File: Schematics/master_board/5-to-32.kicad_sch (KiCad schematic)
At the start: 22 parts, among them J10 Conn_01x06_Male, J11 Conn_01x06_Male, J12 Conn_01x06_Male, J13 Conn_01x06_Male, J14 Conn_01x06_Male, J15 Conn_01x06_Male, J16 Conn_01x06_Male, J17 Conn_01x06_Male, J18 Conn_01x06_Male, J19 Conn_01x06_Male, J20 Conn_01x06_Male, J21 Conn_01x06_Male, J22 Conn_01x06_Male, J23 Conn_01x06_Male, J24 Conn_01x06_Male, J25 Conn_01x06_Male, J26 Conn_01x06_Male, J7 Conn_01x06_Male, J8 Conn_01x06_Male, J9 Conn_01x06_Male, U4 74HCT154PW,118, U5 74HCT154PW,118

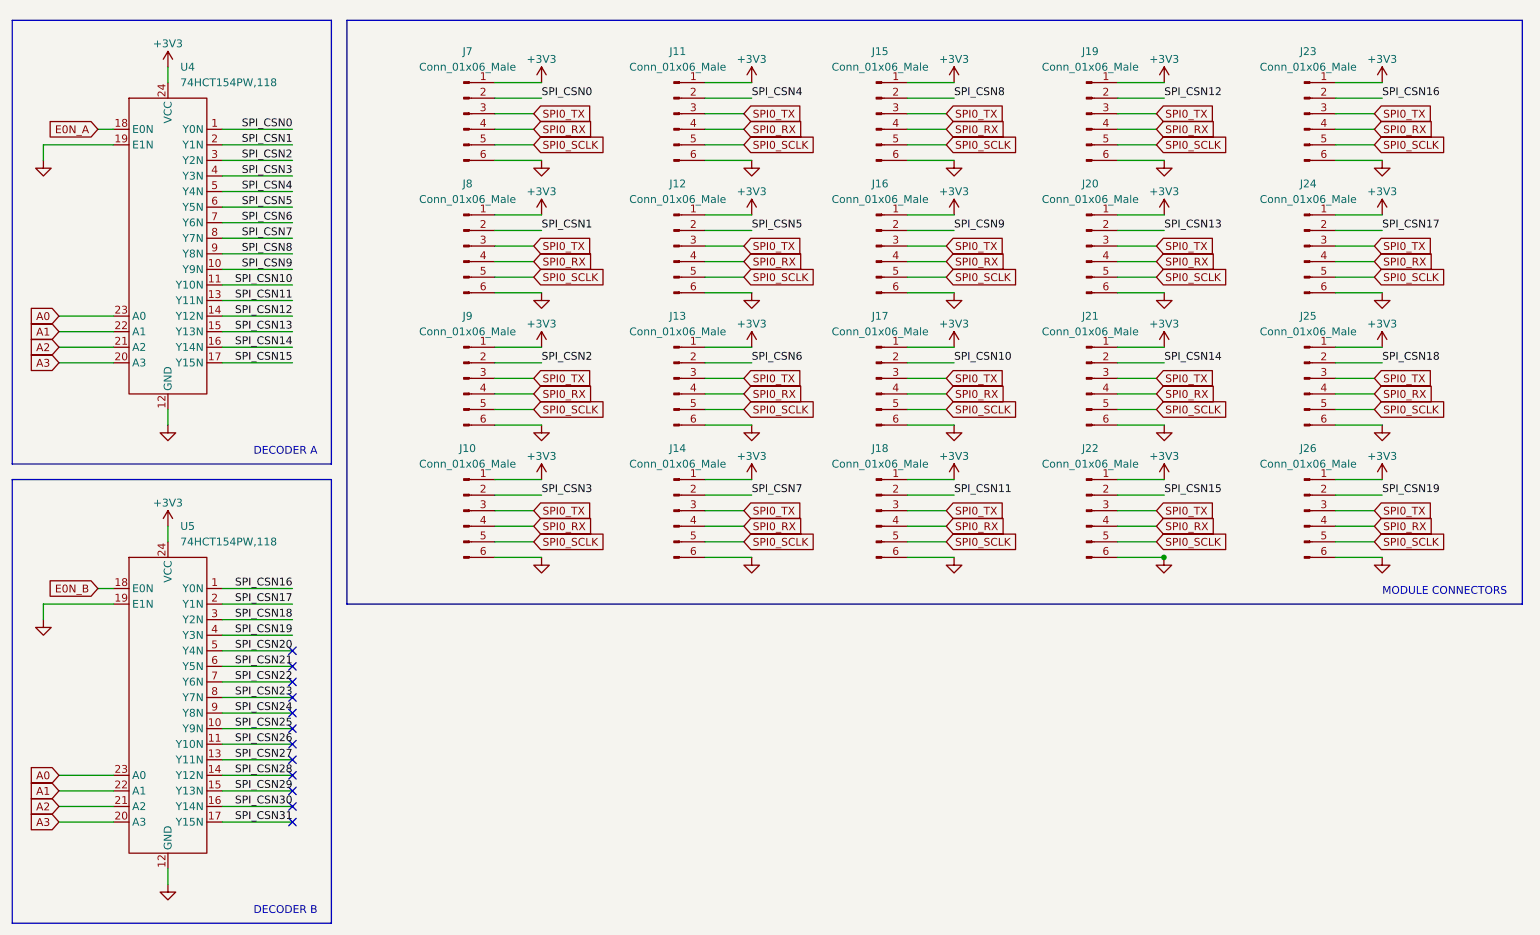
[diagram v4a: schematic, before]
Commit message: Route master board and DRC
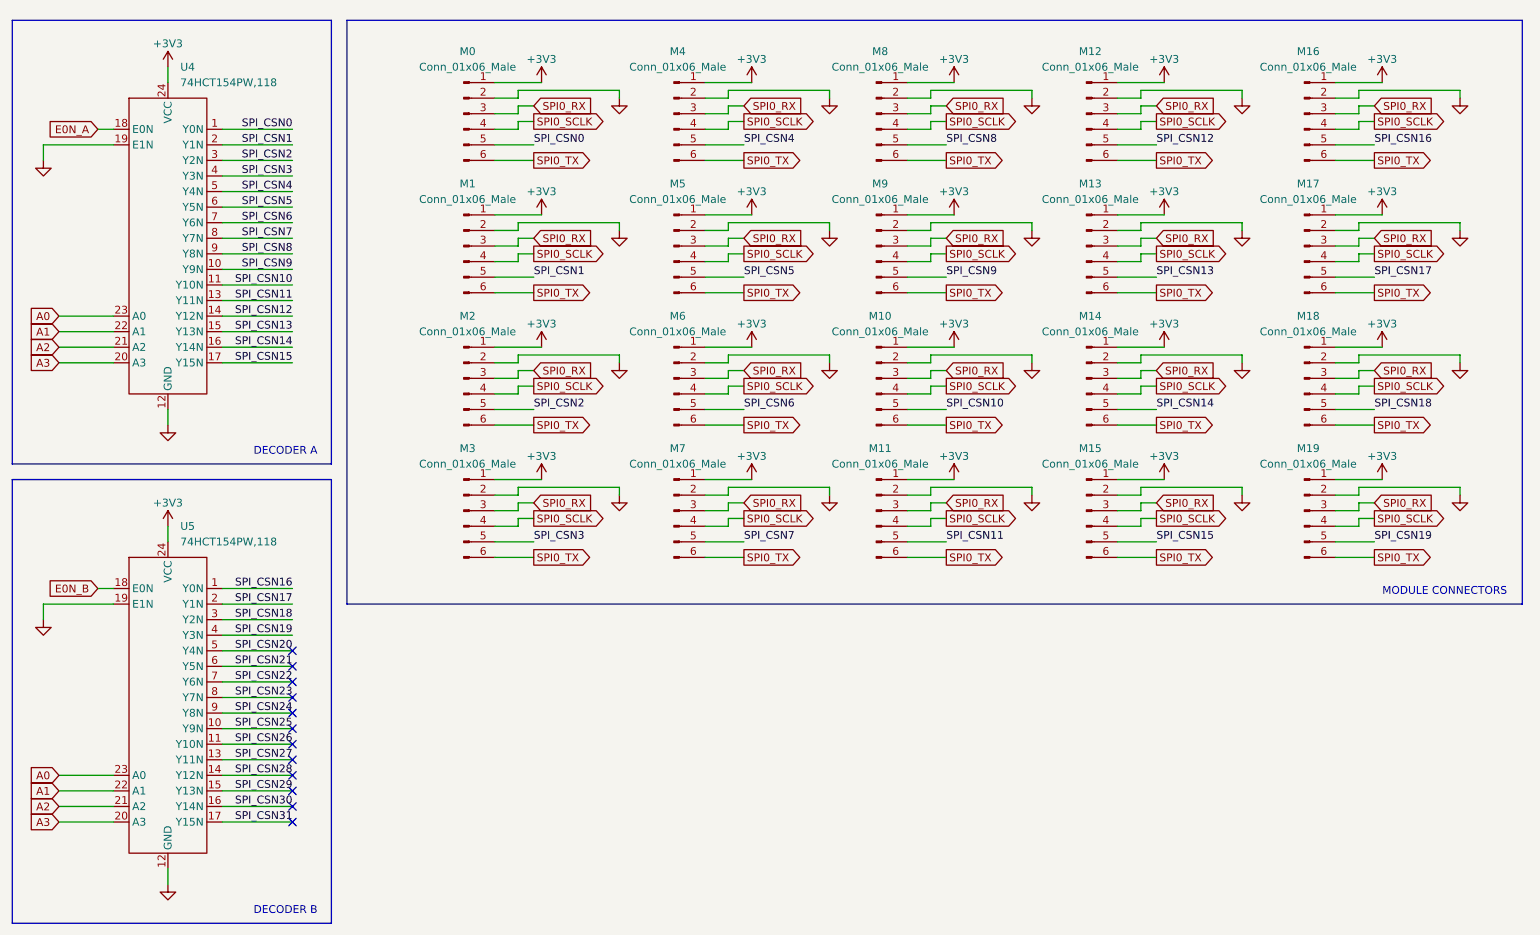
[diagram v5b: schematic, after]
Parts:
- renumbered J7 to M0, J8 to M1, J17 to M10, J18 to M11, J19 to M12, J20 to M13, J21 to M14, J22 to M15, J23 to M16, J24 to M17, J25 to M18, J26 to M19, J9 to M2, J10 to M3, J11 to M4, J12 to M5, J13 to M6, J14 to M7, J15 to M8, J16 to M9
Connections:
- net GND: now also M0.2 (Pin_2), M1.2 (Pin_2), M10.2 (Pin_2), M11.2 (Pin_2), M12.2 (Pin_2), M13.2 (Pin_2), M14.2 (Pin_2), M15.2 (Pin_2), M16.2 (Pin_2), M17.2 (Pin_2), M18.2 (Pin_2), M19.2 (Pin_2), M2.2 (Pin_2), M3.2 (Pin_2), M4.2 (Pin_2), M5.2 (Pin_2), M6.2 (Pin_2), M7.2 (Pin_2), M8.2 (Pin_2), M9.2 (Pin_2); no longer M0.6 (Pin_6), M1.6 (Pin_6), M10.6 (Pin_6), M11.6 (Pin_6), M12.6 (Pin_6), M13.6 (Pin_6), M14.6 (Pin_6), M15.6 (Pin_6), M16.6 (Pin_6), M17.6 (Pin_6), M18.6 (Pin_6), M19.6 (Pin_6), M2.6 (Pin_6), M3.6 (Pin_6), M4.6 (Pin_6), M5.6 (Pin_6), M6.6 (Pin_6), M7.6 (Pin_6), M8.6 (Pin_6), M9.6 (Pin_6)
- net SPI0_RX: now also M0.3 (Pin_3), M1.3 (Pin_3), M10.3 (Pin_3), M11.3 (Pin_3), M12.3 (Pin_3), M13.3 (Pin_3), M14.3 (Pin_3), M15.3 (Pin_3), M16.3 (Pin_3), M17.3 (Pin_3), M18.3 (Pin_3), M19.3 (Pin_3), M2.3 (Pin_3), M3.3 (Pin_3), M4.3 (Pin_3), M5.3 (Pin_3), M6.3 (Pin_3), M7.3 (Pin_3), M8.3 (Pin_3), M9.3 (Pin_3); no longer M0.4 (Pin_4), M1.4 (Pin_4), M10.4 (Pin_4), M11.4 (Pin_4), M12.4 (Pin_4), M13.4 (Pin_4), M14.4 (Pin_4), M15.4 (Pin_4), M16.4 (Pin_4), M17.4 (Pin_4), M18.4 (Pin_4), M19.4 (Pin_4), M2.4 (Pin_4), M3.4 (Pin_4), M4.4 (Pin_4), M5.4 (Pin_4), M6.4 (Pin_4), M7.4 (Pin_4), M8.4 (Pin_4), M9.4 (Pin_4)
- net SPI0_SCLK: now also M0.4 (Pin_4), M1.4 (Pin_4), M10.4 (Pin_4), M11.4 (Pin_4), M12.4 (Pin_4), M13.4 (Pin_4), M14.4 (Pin_4), M15.4 (Pin_4), M16.4 (Pin_4), M17.4 (Pin_4), M18.4 (Pin_4), M19.4 (Pin_4), M2.4 (Pin_4), M3.4 (Pin_4), M4.4 (Pin_4), M5.4 (Pin_4), M6.4 (Pin_4), M7.4 (Pin_4), M8.4 (Pin_4), M9.4 (Pin_4); no longer M0.5 (Pin_5), M1.5 (Pin_5), M10.5 (Pin_5), M11.5 (Pin_5), M12.5 (Pin_5), M13.5 (Pin_5), M14.5 (Pin_5), M15.5 (Pin_5), M16.5 (Pin_5), M17.5 (Pin_5), M18.5 (Pin_5), M19.5 (Pin_5), M2.5 (Pin_5), M3.5 (Pin_5), M4.5 (Pin_5), M5.5 (Pin_5), M6.5 (Pin_5), M7.5 (Pin_5), M8.5 (Pin_5), M9.5 (Pin_5)
- net SPI0_TX: now also M0.6 (Pin_6), M1.6 (Pin_6), M10.6 (Pin_6), M11.6 (Pin_6), M12.6 (Pin_6), M13.6 (Pin_6), M14.6 (Pin_6), M15.6 (Pin_6), M16.6 (Pin_6), M17.6 (Pin_6), M18.6 (Pin_6), M19.6 (Pin_6), M2.6 (Pin_6), M3.6 (Pin_6), M4.6 (Pin_6), M5.6 (Pin_6), M6.6 (Pin_6), M7.6 (Pin_6), M8.6 (Pin_6), M9.6 (Pin_6); no longer M0.3 (Pin_3), M1.3 (Pin_3), M10.3 (Pin_3), M11.3 (Pin_3), M12.3 (Pin_3), M13.3 (Pin_3), M14.3 (Pin_3), M15.3 (Pin_3), M16.3 (Pin_3), M17.3 (Pin_3), M18.3 (Pin_3), M19.3 (Pin_3), M2.3 (Pin_3), M3.3 (Pin_3), M4.3 (Pin_3), M5.3 (Pin_3), M6.3 (Pin_3), M7.3 (Pin_3), M8.3 (Pin_3), M9.3 (Pin_3)
- net SPI_CSN0: now also M0.5 (Pin_5); no longer M0.2 (Pin_2)
- net SPI_CSN1: now also M1.5 (Pin_5); no longer M1.2 (Pin_2)
- net SPI_CSN10: now also M10.5 (Pin_5); no longer M10.2 (Pin_2)
- net SPI_CSN11: now also M11.5 (Pin_5); no longer M11.2 (Pin_2)
- net SPI_CSN12: now also M12.5 (Pin_5); no longer M12.2 (Pin_2)
- net SPI_CSN13: now also M13.5 (Pin_5); no longer M13.2 (Pin_2)
- net SPI_CSN14: now also M14.5 (Pin_5); no longer M14.2 (Pin_2)
- net SPI_CSN15: now also M15.5 (Pin_5); no longer M15.2 (Pin_2)
- net SPI_CSN16: now also M16.5 (Pin_5); no longer M16.2 (Pin_2)
- net SPI_CSN17: now also M17.5 (Pin_5); no longer M17.2 (Pin_2)
- net SPI_CSN18: now also M18.5 (Pin_5); no longer M18.2 (Pin_2)
- net SPI_CSN19: now also M19.5 (Pin_5); no longer M19.2 (Pin_2)
- net SPI_CSN2: now also M2.5 (Pin_5); no longer M2.2 (Pin_2)
- net SPI_CSN3: now also M3.5 (Pin_5); no longer M3.2 (Pin_2)
- net SPI_CSN4: now also M4.5 (Pin_5); no longer M4.2 (Pin_2)
- net SPI_CSN5: now also M5.5 (Pin_5); no longer M5.2 (Pin_2)
- net SPI_CSN6: now also M6.5 (Pin_5); no longer M6.2 (Pin_2)
- net SPI_CSN7: now also M7.5 (Pin_5); no longer M7.2 (Pin_2)
- net SPI_CSN8: now also M8.5 (Pin_5); no longer M8.2 (Pin_2)
- net SPI_CSN9: now also M9.5 (Pin_5); no longer M9.2 (Pin_2)

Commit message: bom generation script
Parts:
- U4, U5: Manufacturer (none) -> Nexperia USA Inc.; Manufacturer Part Number (none) -> 74HCT154PW,118
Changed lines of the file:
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@@
+      (effects (font (size 1.27 1.27)) hide)
+    )
+    (property "Manufacturer" "Nexperia USA Inc." (id 4) (at 54.61 63.5 0)
+      (effects (font (size 1.27 1.27)) hide)
+    )
+    (property "Manufacturer Part Number" "74HCT154PW,118" (id 5) (at 54.61 63.5 0)
       (effects (font (size 1.27 1.27)) hide)
     )
@@
       (effects (font (size 1.27 1.27)) hide)
     )
+    (property "Manufacturer" "Nexperia USA Inc." (id 4) (at 54.61 138.43 0)
+      (effects (font (size 1.27 1.27)) hide)
+    )
+    (property "Manufacturer Part Number" "74HCT154PW,118" (id 5) (at 54.61 138.43 0)
+      (effects (font (size 1.27 1.27)) hide)
+    )

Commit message: Changed 10k res values to 1k, SWD pins, Decoder footprints, and haptic pins
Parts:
- U4, U5: footprint Package_SO:TSSOP-24_4.4x5mm_P0.4mm -> Package_SO:TSSOP-24_4.4x7.8mm_P0.65mm
- renumbered M0 to M1, M9 to M10, M10 to M11, M11 to M12, M12 to M13, M13 to M14, M14 to M15, M15 to M16, M16 to M17, M17 to M18, M18 to M19, M1 to M2, M19 to M20, M2 to M3, M3 to M4, M4 to M5, M5 to M6, M6 to M7, M7 to M8, M8 to M9
